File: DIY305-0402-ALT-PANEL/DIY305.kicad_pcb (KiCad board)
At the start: 2 copper layers, 9.8 x 18.5 mm, 38 parts, among them J1 Conn_01x07, J2 Conn_01x07

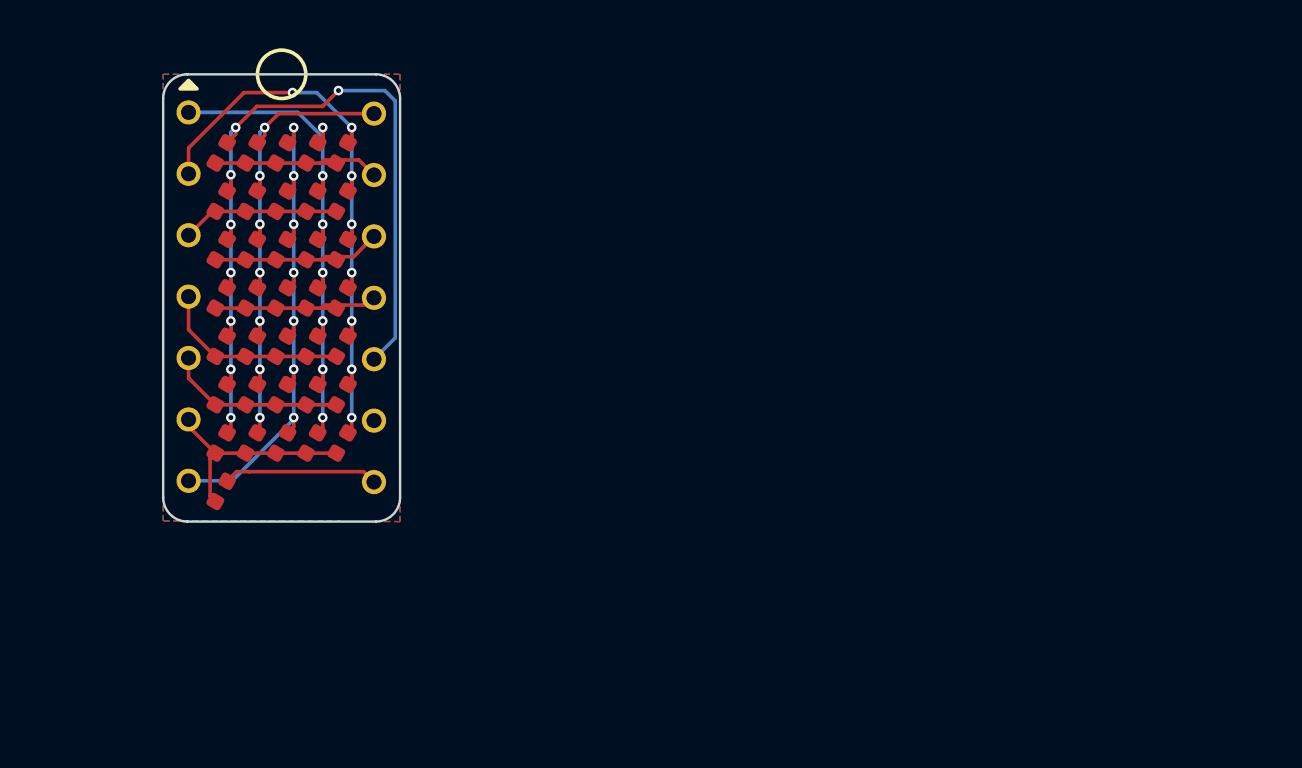
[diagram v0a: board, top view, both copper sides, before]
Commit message: started work on manually paneling the pcb so I can get a more accurate price quote.
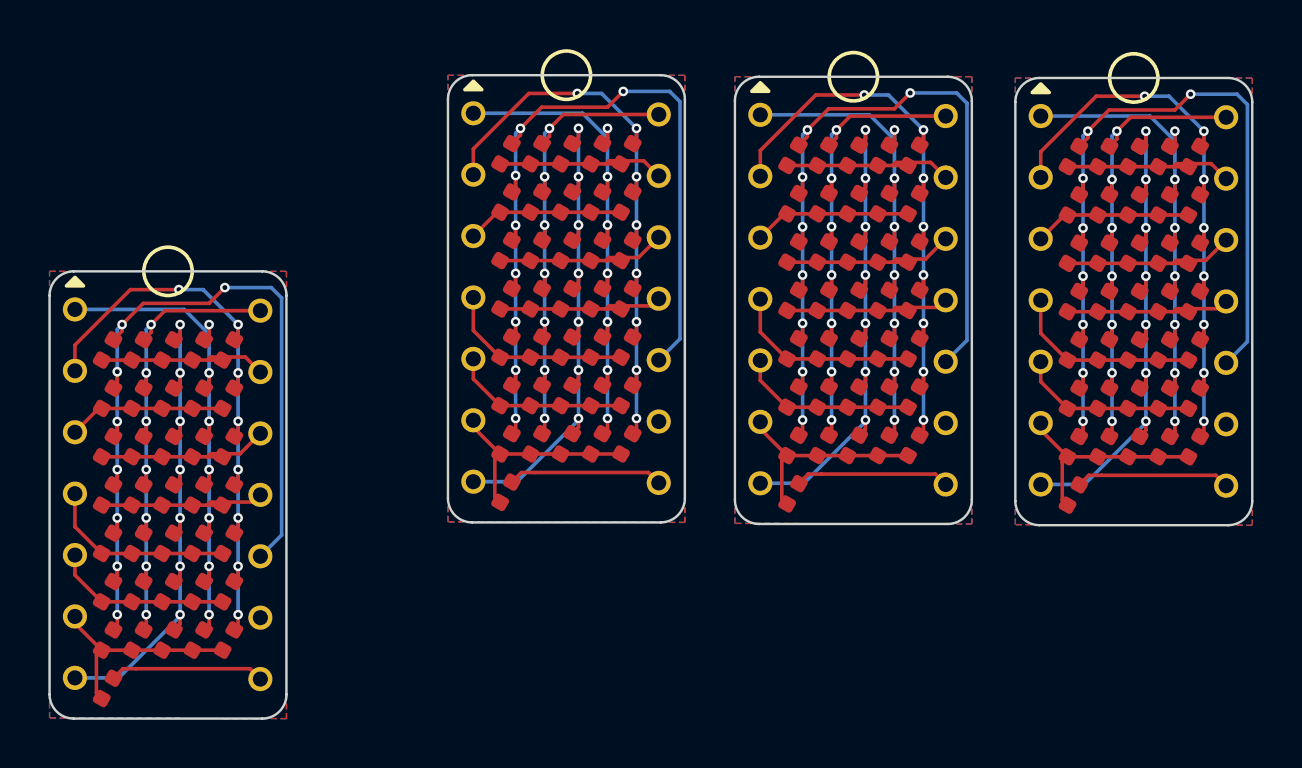
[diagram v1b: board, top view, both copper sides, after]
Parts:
- added D100: LED, LED_SMD:LED_0402_1005Metric, F.Cu at (49.8, 33.4)
- added D101: LED, LED_SMD:LED_0402_1005Metric, F.Cu at (49.8, 35.4)
- added D102: LED, LED_SMD:LED_0402_1005Metric, F.Cu at (51.0, 23.4)
- added D103: LED, LED_SMD:LED_0402_1005Metric, F.Cu at (51.0, 25.4)
- added D104: LED, LED_SMD:LED_0402_1005Metric, F.Cu at (51.0, 27.4)
- added D105: LED, LED_SMD:LED_0402_1005Metric, F.Cu at (51.0, 29.4)
- added D106: LED, LED_SMD:LED_0402_1005Metric, F.Cu at (51.0, 31.4)
- added D107: LED, LED_SMD:LED_0402_1005Metric, F.Cu at (51.0, 33.4)
- added D108: LED, LED_SMD:LED_0402_1005Metric, F.Cu at (51.0, 35.4)
- added D109: LED, LED_SMD:LED_0402_1005Metric, F.Cu at (57.6, 23.4)
- added D110: LED, LED_SMD:LED_0402_1005Metric, F.Cu at (57.6, 25.4)
- added D111: LED, LED_SMD:LED_0402_1005Metric, F.Cu at (57.6, 27.4)
- added D112: LED, LED_SMD:LED_0402_1005Metric, F.Cu at (57.6, 29.4)
- added D113: LED, LED_SMD:LED_0402_1005Metric, F.Cu at (57.6, 31.4)
- added D114: LED, LED_SMD:LED_0402_1005Metric, F.Cu at (57.6, 33.4)
- added D115: LED, LED_SMD:LED_0402_1005Metric, F.Cu at (57.6, 35.4)
- added D116: LED, LED_SMD:LED_0402_1005Metric, F.Cu at (57.6, 37.4)
- added D117: LED, LED_SMD:LED_0402_1005Metric, F.Cu at (58.9, 23.4)
- added D118: LED, LED_SMD:LED_0402_1005Metric, F.Cu at (58.9, 25.4)
- added D119: LED, LED_SMD:LED_0402_1005Metric, F.Cu at (58.9, 27.4)
- added D120: LED, LED_SMD:LED_0402_1005Metric, F.Cu at (58.9, 29.4)
- added D121: LED, LED_SMD:LED_0402_1005Metric, F.Cu at (58.9, 31.4)
- added D122: LED, LED_SMD:LED_0402_1005Metric, F.Cu at (58.9, 33.4)
- added D123: LED, LED_SMD:LED_0402_1005Metric, F.Cu at (58.9, 35.4)
- added D124: LED, LED_SMD:LED_0402_1005Metric, F.Cu at (60.1, 23.4)
- added D125: LED, LED_SMD:LED_0402_1005Metric, F.Cu at (60.1, 25.4)
- added D126: LED, LED_SMD:LED_0402_1005Metric, F.Cu at (60.1, 27.4)
- added D127: LED, LED_SMD:LED_0402_1005Metric, F.Cu at (60.1, 29.4)
- added D128: LED, LED_SMD:LED_0402_1005Metric, F.Cu at (60.1, 31.4)
- added D129: LED, LED_SMD:LED_0402_1005Metric, F.Cu at (60.1, 33.4)
- added D130: LED, LED_SMD:LED_0402_1005Metric, F.Cu at (60.1, 35.4)
- added D131: LED, LED_SMD:LED_0402_1005Metric, F.Cu at (61.4, 23.4)
- added D132: LED, LED_SMD:LED_0402_1005Metric, F.Cu at (61.4, 25.4)
- added D133: LED, LED_SMD:LED_0402_1005Metric, F.Cu at (61.4, 27.4)
- added D134: LED, LED_SMD:LED_0402_1005Metric, F.Cu at (61.4, 29.4)
- added D135: LED, LED_SMD:LED_0402_1005Metric, F.Cu at (61.4, 31.4)
- added D136: LED, LED_SMD:LED_0402_1005Metric, F.Cu at (61.4, 33.4)
- added D137: LED, LED_SMD:LED_0402_1005Metric, F.Cu at (61.4, 35.4)
- added D138: LED, LED_SMD:LED_0402_1005Metric, F.Cu at (62.6, 23.4)
- added D139: LED, LED_SMD:LED_0402_1005Metric, F.Cu at (62.6, 25.4)
- added D140: LED, LED_SMD:LED_0402_1005Metric, F.Cu at (62.6, 27.4)
- added D141: LED, LED_SMD:LED_0402_1005Metric, F.Cu at (62.6, 29.4)
- added D142: LED, LED_SMD:LED_0402_1005Metric, F.Cu at (62.6, 31.4)
- added D143: LED, LED_SMD:LED_0402_1005Metric, F.Cu at (62.6, 33.4)
- added D144: LED, LED_SMD:LED_0402_1005Metric, F.Cu at (62.6, 35.4)
- added D37: LED, LED_SMD:LED_0402_1005Metric, F.Cu at (34.2, 23.3)
- added D38: LED, LED_SMD:LED_0402_1005Metric, F.Cu at (34.2, 25.3)
- added D39: LED, LED_SMD:LED_0402_1005Metric, F.Cu at (34.2, 27.3)
- added D40: LED, LED_SMD:LED_0402_1005Metric, F.Cu at (34.2, 29.3)
- added D41: LED, LED_SMD:LED_0402_1005Metric, F.Cu at (34.2, 31.3)
- added D42: LED, LED_SMD:LED_0402_1005Metric, F.Cu at (34.2, 33.3)
- added D43: LED, LED_SMD:LED_0402_1005Metric, F.Cu at (34.2, 35.3)
- added D44: LED, LED_SMD:LED_0402_1005Metric, F.Cu at (34.2, 37.3)
- added D45: LED, LED_SMD:LED_0402_1005Metric, F.Cu at (35.4, 23.3)
- added D46: LED, LED_SMD:LED_0402_1005Metric, F.Cu at (35.4, 25.3)
- added D47: LED, LED_SMD:LED_0402_1005Metric, F.Cu at (35.4, 27.3)
- added D48: LED, LED_SMD:LED_0402_1005Metric, F.Cu at (35.4, 29.3)
- added D49: LED, LED_SMD:LED_0402_1005Metric, F.Cu at (35.4, 31.3)
- added D50: LED, LED_SMD:LED_0402_1005Metric, F.Cu at (35.4, 33.3)
- added D51: LED, LED_SMD:LED_0402_1005Metric, F.Cu at (35.4, 35.3)
- added D52: LED, LED_SMD:LED_0402_1005Metric, F.Cu at (36.7, 23.3)
- added D53: LED, LED_SMD:LED_0402_1005Metric, F.Cu at (36.7, 25.3)
- added D54: LED, LED_SMD:LED_0402_1005Metric, F.Cu at (36.7, 27.3)
- added D55: LED, LED_SMD:LED_0402_1005Metric, F.Cu at (36.7, 29.3)
- added D56: LED, LED_SMD:LED_0402_1005Metric, F.Cu at (36.7, 31.3)
- added D57: LED, LED_SMD:LED_0402_1005Metric, F.Cu at (36.7, 33.3)
- added D58: LED, LED_SMD:LED_0402_1005Metric, F.Cu at (36.7, 35.3)
- added D59: LED, LED_SMD:LED_0402_1005Metric, F.Cu at (37.9, 23.3)
- added D60: LED, LED_SMD:LED_0402_1005Metric, F.Cu at (37.9, 25.3)
- added D61: LED, LED_SMD:LED_0402_1005Metric, F.Cu at (37.9, 27.3)
- added D62: LED, LED_SMD:LED_0402_1005Metric, F.Cu at (37.9, 29.3)
- added D63: LED, LED_SMD:LED_0402_1005Metric, F.Cu at (37.9, 31.3)
- added D64: LED, LED_SMD:LED_0402_1005Metric, F.Cu at (37.9, 33.3)
- added D65: LED, LED_SMD:LED_0402_1005Metric, F.Cu at (37.9, 35.3)
- added D66: LED, LED_SMD:LED_0402_1005Metric, F.Cu at (39.2, 23.3)
- added D67: LED, LED_SMD:LED_0402_1005Metric, F.Cu at (39.2, 25.3)
- added D68: LED, LED_SMD:LED_0402_1005Metric, F.Cu at (39.2, 27.3)
- added D69: LED, LED_SMD:LED_0402_1005Metric, F.Cu at (39.2, 29.3)
- added D70: LED, LED_SMD:LED_0402_1005Metric, F.Cu at (39.2, 31.3)
- added D71: LED, LED_SMD:LED_0402_1005Metric, F.Cu at (39.2, 33.3)
- added D72: LED, LED_SMD:LED_0402_1005Metric, F.Cu at (39.2, 35.3)
- added D73: LED, LED_SMD:LED_0402_1005Metric, F.Cu at (46.0, 23.4)
- added D74: LED, LED_SMD:LED_0402_1005Metric, F.Cu at (46.0, 25.4)
- added D75: LED, LED_SMD:LED_0402_1005Metric, F.Cu at (46.0, 27.4)
- added D76: LED, LED_SMD:LED_0402_1005Metric, F.Cu at (46.0, 29.4)
- added D77: LED, LED_SMD:LED_0402_1005Metric, F.Cu at (46.0, 31.4)
- added D78: LED, LED_SMD:LED_0402_1005Metric, F.Cu at (46.0, 33.4)
- added D79: LED, LED_SMD:LED_0402_1005Metric, F.Cu at (46.0, 35.4)
- added D80: LED, LED_SMD:LED_0402_1005Metric, F.Cu at (46.0, 37.4)
- added D81: LED, LED_SMD:LED_0402_1005Metric, F.Cu at (47.3, 23.4)
- added D82: LED, LED_SMD:LED_0402_1005Metric, F.Cu at (47.3, 25.4)
- added D83: LED, LED_SMD:LED_0402_1005Metric, F.Cu at (47.3, 27.4)
- added D84: LED, LED_SMD:LED_0402_1005Metric, F.Cu at (47.3, 29.4)
- added D85: LED, LED_SMD:LED_0402_1005Metric, F.Cu at (47.3, 31.4)
- added D86: LED, LED_SMD:LED_0402_1005Metric, F.Cu at (47.3, 33.4)
- added D87: LED, LED_SMD:LED_0402_1005Metric, F.Cu at (47.3, 35.4)
- added D88: LED, LED_SMD:LED_0402_1005Metric, F.Cu at (48.5, 23.4)
- added D89: LED, LED_SMD:LED_0402_1005Metric, F.Cu at (48.5, 25.4)
- added D90: LED, LED_SMD:LED_0402_1005Metric, F.Cu at (48.5, 27.4)
- added D91: LED, LED_SMD:LED_0402_1005Metric, F.Cu at (48.5, 29.4)
- added D92: LED, LED_SMD:LED_0402_1005Metric, F.Cu at (48.5, 31.4)
- added D93: LED, LED_SMD:LED_0402_1005Metric, F.Cu at (48.5, 33.4)
- added D94: LED, LED_SMD:LED_0402_1005Metric, F.Cu at (48.5, 35.4)
- added D95: LED, LED_SMD:LED_0402_1005Metric, F.Cu at (49.8, 23.4)
- added D96: LED, LED_SMD:LED_0402_1005Metric, F.Cu at (49.8, 25.4)
- added D97: LED, LED_SMD:LED_0402_1005Metric, F.Cu at (49.8, 27.4)
- added D98: LED, LED_SMD:LED_0402_1005Metric, F.Cu at (49.8, 29.4)
- added D99: LED, LED_SMD:LED_0402_1005Metric, F.Cu at (49.8, 31.4)
- added J3: Conn_01x07, Connector_PinHeader_2.54mm:PinHeader_1x07_P2.54mm_Vertical, F.Cu at (32.8, 21.6)
- added J4: Conn_01x07, Connector_PinHeader_2.54mm:PinHeader_1x07_P2.54mm_Vertical, F.Cu at (40.5, 21.7)
- added J5: Conn_01x07, Connector_PinHeader_2.54mm:PinHeader_1x07_P2.54mm_Vertical, F.Cu at (44.7, 21.7)
- added J6: Conn_01x07, Connector_PinHeader_2.54mm:PinHeader_1x07_P2.54mm_Vertical, F.Cu at (52.4, 21.7)
- added J7: Conn_01x07, Connector_PinHeader_2.54mm:PinHeader_1x07_P2.54mm_Vertical, F.Cu at (56.3, 21.7)
- added J8: Conn_01x07, Connector_PinHeader_2.54mm:PinHeader_1x07_P2.54mm_Vertical, F.Cu at (64.0, 21.8)
- moved J1 9.41 mm to (16.4, 29.7)
- moved D1 9.41 mm to (17.7, 31.4)
- moved D10 9.41 mm to (18.9, 33.4)
- moved D11 9.41 mm to (18.9, 35.4)
- moved D12 9.41 mm to (18.9, 37.4)
- moved D13 9.41 mm to (18.9, 39.4)
- moved D14 9.41 mm to (18.9, 41.4)
- moved D15 9.41 mm to (18.9, 43.4)
- moved D16 9.41 mm to (20.2, 31.4)
- moved D17 9.41 mm to (20.2, 33.4)
- moved D18 9.41 mm to (20.2, 35.4)
- moved D19 9.41 mm to (20.2, 37.4)
- moved D2 9.41 mm to (17.7, 33.4)
- moved D20 9.41 mm to (20.2, 39.4)
- moved D21 9.41 mm to (20.2, 41.4)
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- renumbered D9 to D10, D10 to D11, D11 to D12, D12 to D13, D13 to D14, D14 to D15, D15 to D16, D16 to D17, D17 to D18, D18 to D19, D19 to D20, D20 to D21, D21 to D22, D22 to D23, D23 to D24, D24 to D25, D25 to D26, D26 to D27, D27 to D28, D28 to D29, D29 to D30, D30 to D31, D31 to D32, D32 to D33, D33 to D34, D34 to D35, D35 to D36, D36 to D8, D8 to D9
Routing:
- net C1: track 35.5 -> 142.1 mm, vias 8 -> 32
- net C5: track 26.2 -> 104.9 mm, vias 8 -> 32
- net C4: track 23.0 -> 92.0 mm, vias 7 -> 28
- net C3: track 22.6 -> 90.5 mm, vias 7 -> 28
- net C2: track 21.6 -> 86.6 mm, vias 7 -> 28
- net R7: track 9.03 -> 36.1 mm
- net R5: track 7.93 -> 31.7 mm
- net R3: track 7.59 -> 30.3 mm
- net R1: track 7.50 -> 30.0 mm
- net R6: track 7.39 -> 29.6 mm
- net R4: track 7.36 -> 29.5 mm
- net R2: track 6.52 -> 26.1 mm
- net DP: track 6.42 -> 25.7 mm
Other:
- board size 9.8 x 18.5 mm -> 49.8 x 26.6 mm
